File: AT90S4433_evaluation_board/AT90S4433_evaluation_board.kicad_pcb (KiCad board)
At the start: 2 copper layers, 12 parts

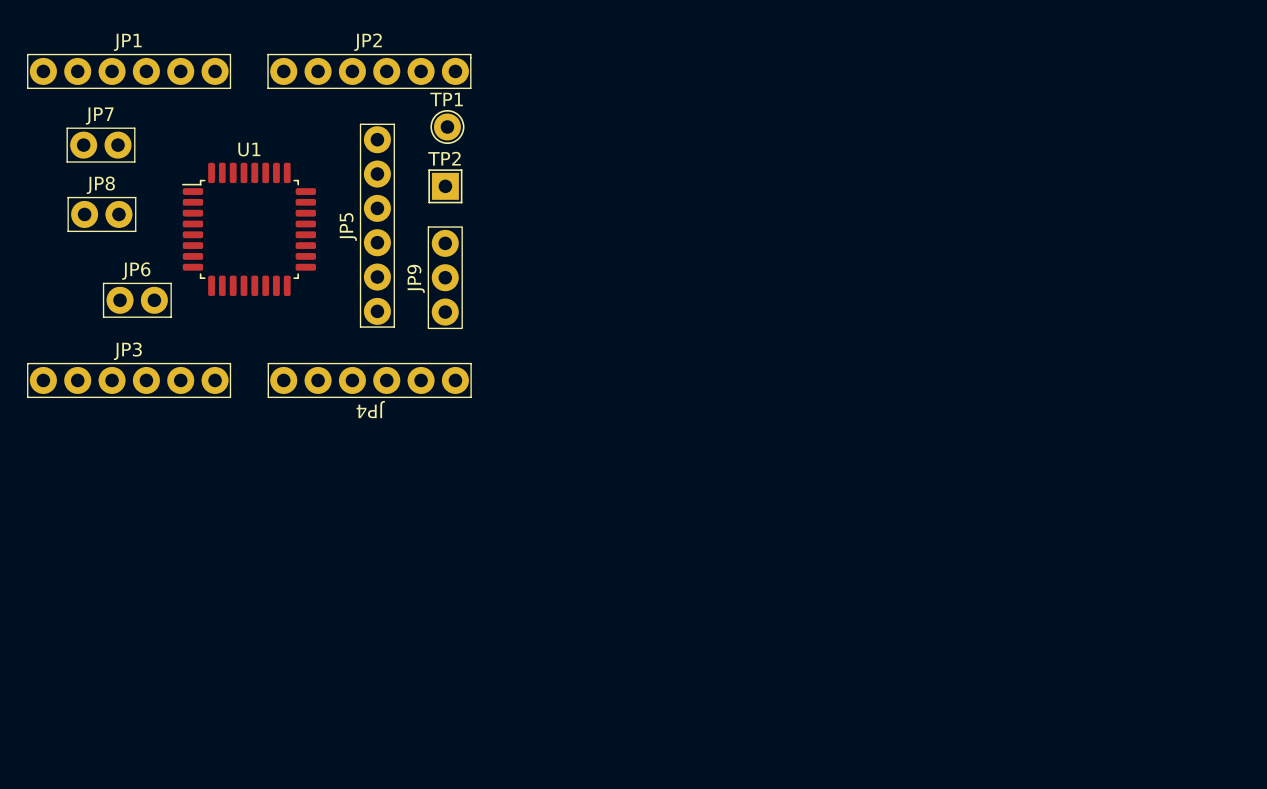
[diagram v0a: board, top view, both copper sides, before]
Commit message: initial footprints for all components, modified layout
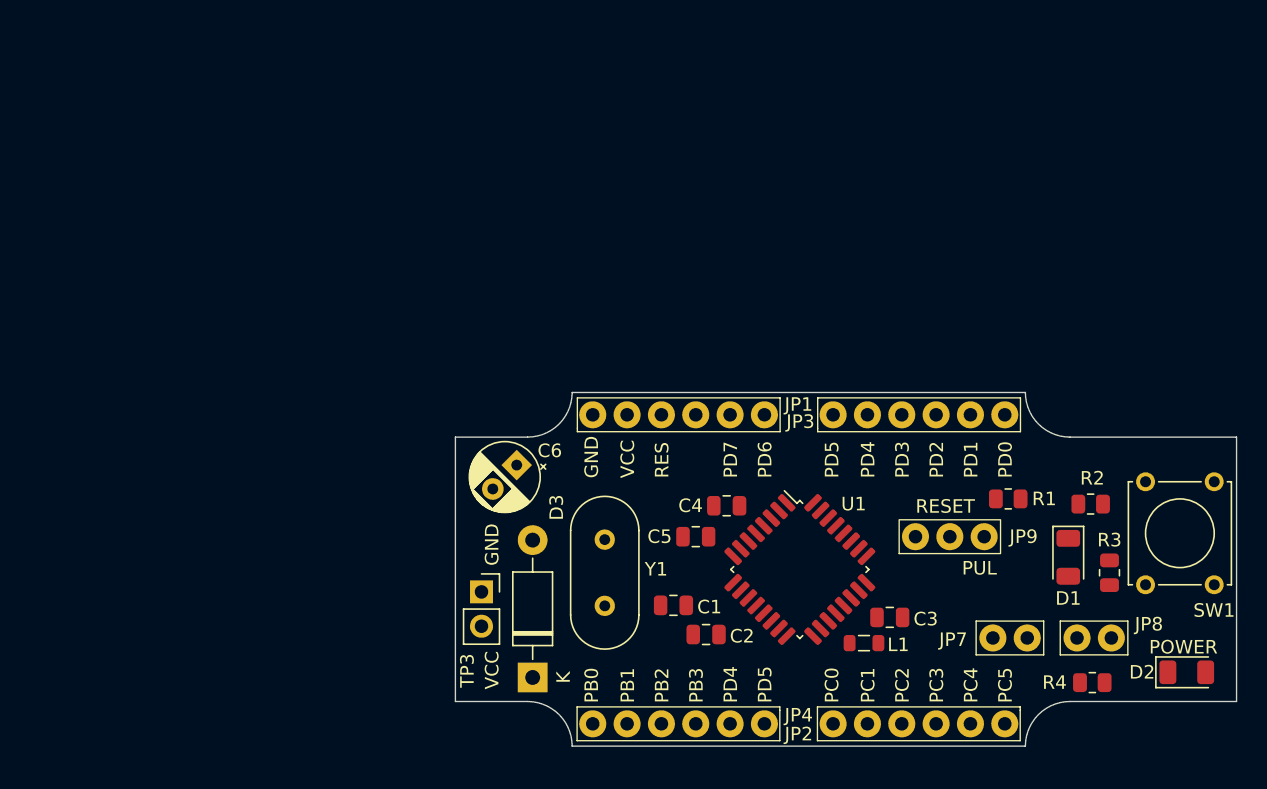
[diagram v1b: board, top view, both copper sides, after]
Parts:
- removed JP5: ~, project_lib_footprints:breadboard_pins
- removed JP6: PWR_LED_jumper, project_lib_footprints:2_pin_jumper_socket
- removed TP1: TestPoint, TestPoint:TestPoint_THTPad_D2.0mm_Drill1.0mm
- removed TP2: TestPoint, TestPoint:TestPoint_THTPad_2.0x2.0mm_Drill1.0mm
- added C1: C, Capacitor_SMD:C_0805_2012Metric, F.Cu at (115.2, 90.3)
- added C2: C, Capacitor_SMD:C_0805_2012Metric, F.Cu at (117.6, 92.5)
- added C3: C, Capacitor_SMD:C_0805_2012Metric, F.Cu at (131.2, 91.2)
- added C4: C, Capacitor_SMD:C_0805_2012Metric, F.Cu at (119.1, 82.9)
- added C5: C, Capacitor_SMD:C_0805_2012Metric, F.Cu at (116.8, 85.2)
- added C6: C_Polarized, Capacitor_THT:CP_Radial_D5.0mm_P2.50mm, F.Cu at (103.6, 79.9)
- added D1: USR_LED, LED_SMD:LED_1206_3216Metric, F.Cu at (144.4, 86.7)
- added D2: PWR_LED, LED_SMD:LED_1206_3216Metric, F.Cu at (153.2, 95.2)
- added D3: 1N4001, Diode_THT:D_DO-41_SOD81_P10.16mm_Horizontal, F.Cu at (104.8, 95.6)
- added L1: L, Inductor_SMD:L_0805_2012Metric, F.Cu at (129.3, 93.1)
- added R1: R, Resistor_SMD:R_0805_2012Metric, F.Cu at (140.0, 82.4)
- added R2: R, Resistor_SMD:R_0805_2012Metric, F.Cu at (146.1, 82.8)
- added R3: R, Resistor_SMD:R_0805_2012Metric, F.Cu at (147.4, 87.9)
- added R4: R, Resistor_SMD:R_0805_2012Metric, F.Cu at (146.2, 96.0)
- added SW1: USR_BTN, Button_Switch_THT:SW_Tactile_Straight_KSA0Axx1LFTR, F.Cu at (155.2, 81.2)
- added TP3: TestPoint_2Pole, Connector_PinSocket_2.54mm:PinSocket_1x02_P2.54mm_Vertical, F.Cu at (101.0, 89.3)
- added Y1: Crystal_Small, Crystal:Crystal_HC18-U_Vertical, F.Cu at (110.1, 90.3)
- moved JP8 79.8 mm to (146.3, 92.7), turned to 180 degrees
- moved JP7 76.5 mm to (140.1, 92.7), turned to 180 degrees
- moved JP2 63.1 mm to (133.3, 99.1)
- moved JP3 58.5 mm to (133.4, 76.2), turned to 180 degrees
- moved JP1 47.9 mm to (115.6, 76.2), turned to 180 degrees
- moved U1 47.9 mm to (124.5, 87.6), turned to -45 degrees
- moved JP9 42.0 mm to (135.6, 85.2), turned to 180 degrees
- moved JP4 34.2 mm to (115.6, 99.1), turned to 0 degrees
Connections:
- JP1 pad 4: unconnected-(JP1-Pad4) -> /EXT_RESET
- JP9 pad 3: /RESET -> /EXT_RESET
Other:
- board outline added: 57.8 x 26.2 mm
- board text added: "GND"
- board text added: "MISO"
- board text added: "MOSI"
- board text added: "PB0"
- board text added: "PB1"
- board text added: "PB2"
- board text added: "PB3"
- board text added: "PC0"
- board text added: "PC1"
- board text added: "PC2"
- board text added: "PC3"
- board text added: "PC4"
- board text added: "PC5"
- board text added: "PD0"
- board text added: "PD1"
- board text added: "PD2"
- board text added: "PD3"
- board text added: "PD4"
- board text added: "PD5"
- board text added: "PD6"
- board text added: "PD7"
- board text added: "POWER"
- board text added: "PUL"
- board text added: "RES"
- board text added: "RESET"
- board text added: "RXD"
- board text added: "SCK"
- board text added: "TXD"
- board text added: "USR_BTN"
- board text added: "USR_LED"
- board text added: "VCC"

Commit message: first routes
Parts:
- TP3: footprint Connector_PinSocket_2.54mm:PinSocket_1x02_P2.54mm_Vertical -> project_lib_footprints:Power_socker
- moved D1 10.5 mm to (153.7, 91.7), turned to 0 degrees
- moved SW1 9.50 mm to (145.8, 79.8), turned to 0 degrees
- moved JP8 7.38 mm to (138.9, 92.2)
- moved JP7 5.74 mm to (145.8, 92.2)
- moved R2 5.74 mm to (148.7, 87.9), turned to 0 degrees
- moved R3 5.21 mm to (142.2, 87.9), turned to 180 degrees
- moved C5 1.46 mm to (115.4, 85.2)
- moved TP3 1.22 mm to (101.5, 90.4), turned to -90 degrees
- moved R4 1.17 mm to (147.3, 95.8)
- moved D2 0.72 mm to (153.7, 95.8)
- moved D3 0.53 mm to (105.3, 95.7)
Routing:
- net /XTAL2: track 0.00 -> 19.9 mm
- net /PB0: track 0.00 -> 15.7 mm, vias 0 -> 1
- net /XTAL1: track 0.00 -> 15.3 mm
- net /PB1: track 0.00 -> 13.5 mm
- net VCC: track 0.00 -> 11.3 mm, vias 0 -> 3
- net /PB2(SS): track 0.00 -> 11.3 mm
- net /PB3(MOSI): track 0.00 -> 9.60 mm
- net GND: track 0.00 -> 9.00 mm
- net /PB4(MISO): track 0.00 -> 8.22 mm
- net /PB5(SCK): track 0.00 -> 7.97 mm
- added copper zone on F.Cu, net GND
- added copper zone on B.Cu, net VCC
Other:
- board text added: "BTN"
- board text added: "EXT"
- board text added: "LED"
- board text added: "USER"

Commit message: completed routing
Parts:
- moved C3 1.41 mm to (132.5, 90.8)
- moved L1 0.39 mm to (129.2, 93.5)
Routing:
- net VCC: track 11.3 -> 47.4 mm, vias 3 -> 18
- net /PC4(LED): track 0.00 -> 33.2 mm, vias 0 -> 1
- net /PC5(BTN): track 0.00 -> 25.0 mm, vias 0 -> 1
- net /EXT_RESET: track 0.00 -> 22.5 mm
- net /PD5: track 0.00 -> 21.6 mm, vias 0 -> 3
- net /PD7(AIN1): track 0.00 -> 21.5 mm, vias 0 -> 3
- net /PD6(AIN0): track 0.00 -> 19.4 mm, vias 0 -> 3
- net /PC3: track 0.00 -> 18.5 mm, vias 0 -> 1
- net Net-(JP8-A): track 0.00 -> 18.1 mm
- net /PD0(RXD): track 0.00 -> 16.2 mm
- net /PC1: track 0.00 -> 15.1 mm, vias 0 -> 1
- net /PD1(TXD): track 0.00 -> 14.0 mm
- net /PC2: track 0.00 -> 14.0 mm, vias 0 -> 1
- net /PC0: track 0.00 -> 12.8 mm, vias 0 -> 1
- net /PD2: track 0.00 -> 11.8 mm
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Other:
- board size 57.8 x 26.2 mm -> 57.8 x 28.3 mm

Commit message: corrections
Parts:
- added R5: R, Resistor_SMD:R_0805_2012Metric, F.Cu at (106.0, 86.2)
- D3: footprint Diode_THT:D_DO-41_SOD81_P10.16mm_Horizontal -> Diode_SMD:D_2512_6332Metric
- moved D3 3.61 mm to (105.1, 92.0), turned to -90 degrees
- moved TP3 0.61 mm to (100.9, 90.5)
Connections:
- D3 pad 1: VCC -> Net-(D3-K)
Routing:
- net VCC: track 47.4 -> 50.9 mm, vias 18 -> 21
- net Net-(D3-K): track 0.00 -> 2.44 mm

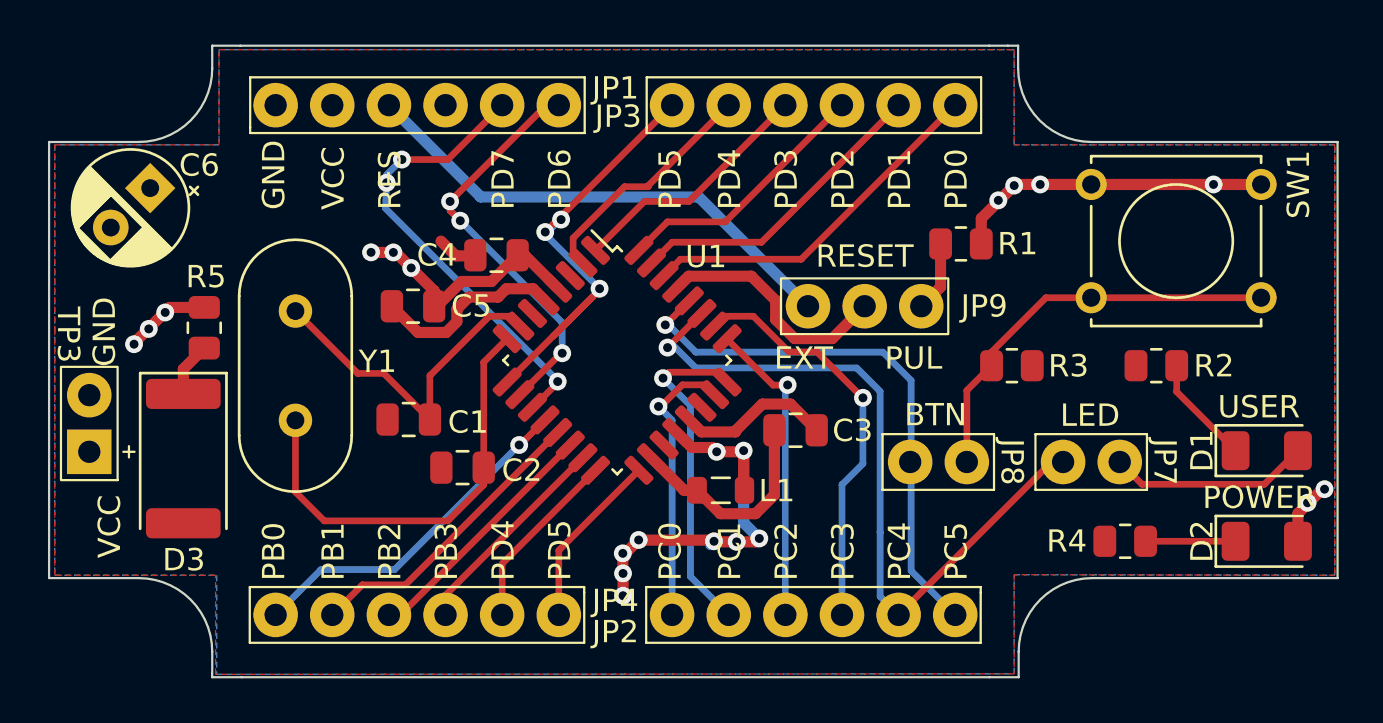
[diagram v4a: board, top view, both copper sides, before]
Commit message: footprint name changes, vias corrections, description
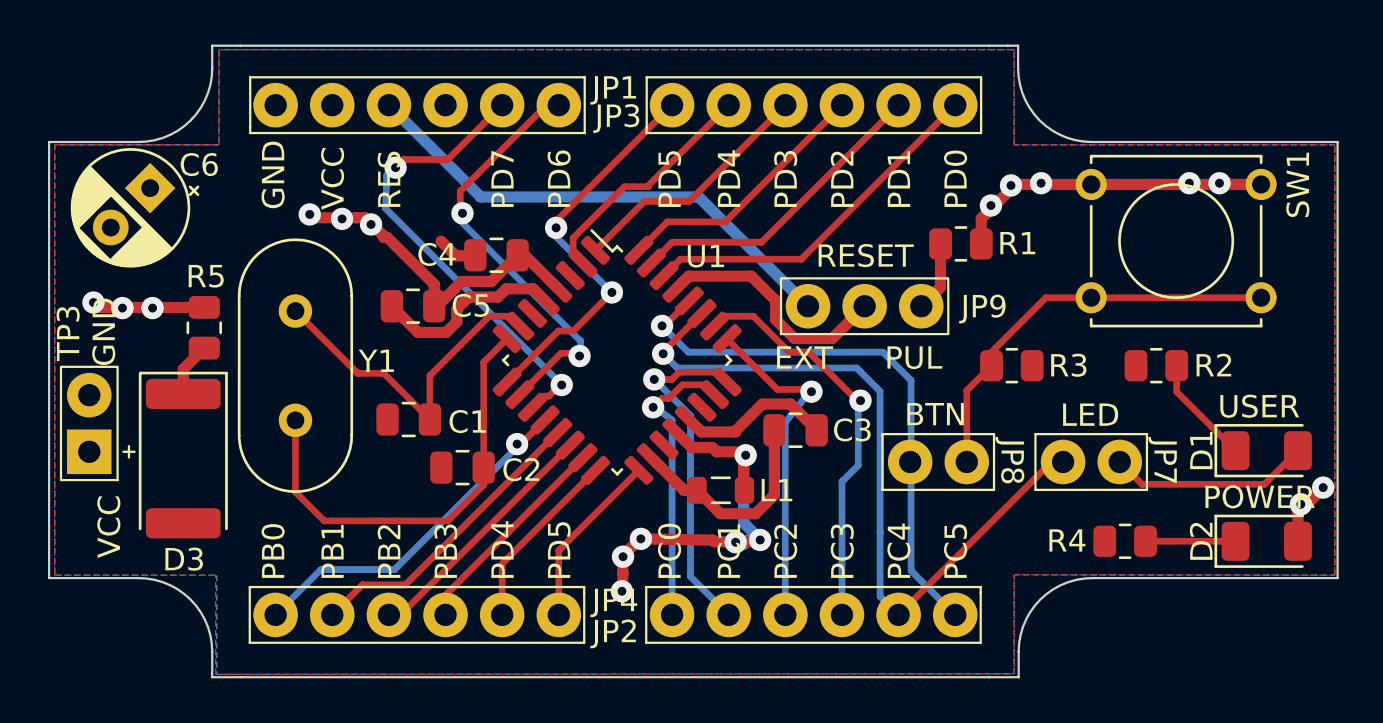
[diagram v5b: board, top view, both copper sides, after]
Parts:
- JP9: footprint project_lib_footprints:3_pin_jumper_socker -> project_lib_footprints:3_pin_jumper_socket
- TP3: footprint project_lib_footprints:Power_socker -> project_lib_footprints:Power_socket
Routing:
- net VCC: track 50.9 -> 58.9 mm, vias 21 -> 19
- net /PD5: track 21.6 -> 18.2 mm, vias 3 -> 2
- net /PC2: track 14.0 -> 15.5 mm
- net /PC1: track 15.1 -> 15.9 mm
- net /PC0: track 12.8 -> 13.6 mm
- net /PD7(AIN1): track 21.5 -> 22.1 mm, vias 3 -> 2
- net /PD6(AIN0): track 19.4 -> 19.7 mm, vias 3 -> 2
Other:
- board text added: "AT90S4433 evaluation board"

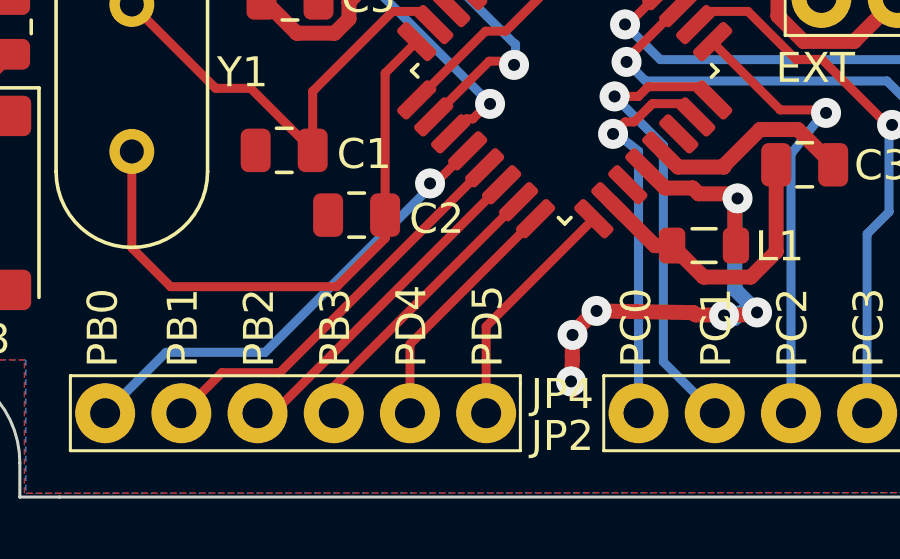
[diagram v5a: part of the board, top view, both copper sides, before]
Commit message: pins description fixes
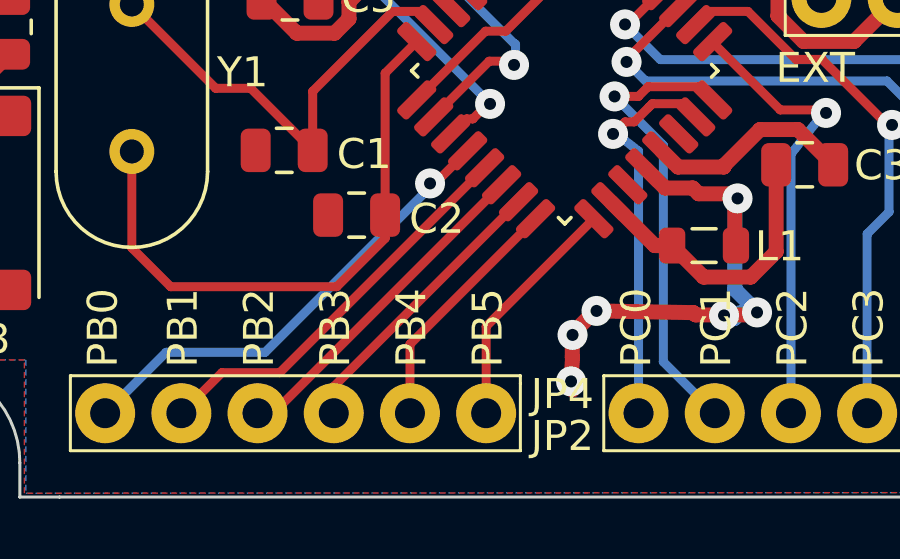
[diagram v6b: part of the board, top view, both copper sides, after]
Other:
- board text added: "PB4"
- board text added: "PB5"
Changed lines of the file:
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@@
     (effects (font (size 1 1) (thickness 0.15)) (justify left bottom))
   )
-  (gr_text "PD4" (at 120.015 97.536 90) (layer "F.SilkS")
+  (gr_text "PB4" (at 120.015 97.536 90) (layer "F.SilkS")
     (effects (font (size 1 1) (thickness 0.15)) (justify left bottom))
   )
@@
     (effects (font (size 1 1) (thickness 0.15)) (justify left bottom))
   )
-  (gr_text "PD5" (at 122.555 97.536 90) (layer "F.SilkS")
+  (gr_text "PB5" (at 122.555 97.536 90) (layer "F.SilkS")
     (effects (font (size 1 1) (thickness 0.15)) (justify left bottom))
   )
